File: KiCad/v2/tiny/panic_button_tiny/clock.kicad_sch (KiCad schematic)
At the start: 6 parts, among them Y3 C3E40000121010X, Y4 CTS3-32.768-12.5-20-R

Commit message: [UPDATE] the schematics annotations
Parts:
- renumbered C15 to C11, C16 to C12, C17 to C13, C18 to C14, Y3 to Y1, Y4 to Y2
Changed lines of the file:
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@@
 		(dnp no)
 		(fields_autoplaced yes)
-		(property "Reference" "C16"
+		(property "Reference" "C12"
 			(at 34.2963 63.5 90)
 			(show_name no)
@@
 			(project "panic_button_tiny"
 				(path "/c4eb92e9-b42f-4db0-b1d9-0ef70f7ca601/525ab16f-d6f3-4728-a011-f4f1ced9fd5e/8e1dfb47-dddf-402c-b136-8c72d0253a57"
-					(reference "C16")
+					(reference "C12")
 					(unit 1)
 				)
@@
 		(in_pos_files yes)
 		(dnp no)
-		(property "Reference" "Y3"
+		(property "Reference" "Y1"
 			(at 38.1 44.45 0)
 			(show_name no)
@@
 			(project "panic_button_tiny"
 				(path "/c4eb92e9-b42f-4db0-b1d9-0ef70f7ca601/525ab16f-d6f3-4728-a011-f4f1ced9fd5e/8e1dfb47-dddf-402c-b136-8c72d0253a57"
-					(reference "Y3")
+					(reference "Y1")
 					(unit 1)
 				)
@@
 		(dnp no)
 		(fields_autoplaced yes)
-		(property "Reference" "#PWR074"
+		(property "Reference" "#PWR072"
 			(at 38.1 83.82 0)
 			(hide yes)
@@
 			(project "panic_button_tiny"
 				(path "/c4eb92e9-b42f-4db0-b1d9-0ef70f7ca601/525ab16f-d6f3-4728-a011-f4f1ced9fd5e/8e1dfb47-dddf-402c-b136-8c72d0253a57"
-					(reference "#PWR074")
+					(reference "#PWR072")
 					(unit 1)
 				)
@@
 		(dnp no)
 		(fields_autoplaced yes)
-		(property "Reference" "C18"
+		(property "Reference" "C14"
 			(at 45.7263 27.94 90)
 			(show_name no)
@@
 			(project "panic_button_tiny"
 				(path "/c4eb92e9-b42f-4db0-b1d9-0ef70f7ca601/525ab16f-d6f3-4728-a011-f4f1ced9fd5e/8e1dfb47-dddf-402c-b136-8c72d0253a57"
-					(reference "C18")
+					(reference "C14")
 					(unit 1)
 				)
@@
 		(in_pos_files yes)
 		(dnp no)
-		(property "Reference" "Y4"
+		(property "Reference" "Y2"
 			(at 39.37 23.368 0)
 			(show_name no)
@@
 			(project "panic_button_tiny"
 				(path "/c4eb92e9-b42f-4db0-b1d9-0ef70f7ca601/525ab16f-d6f3-4728-a011-f4f1ced9fd5e/8e1dfb47-dddf-402c-b136-8c72d0253a57"
-					(reference "Y4")
+					(reference "Y2")
 					(unit 1)
 				)
@@
 		(dnp no)
 		(fields_autoplaced yes)
-		(property "Reference" "#PWR075"
+		(property "Reference" "#PWR073"
 			(at 39.37 33.02 0)
 			(hide yes)
@@
 			(project "panic_button_tiny"
 				(path "/c4eb92e9-b42f-4db0-b1d9-0ef70f7ca601/525ab16f-d6f3-4728-a011-f4f1ced9fd5e/8e1dfb47-dddf-402c-b136-8c72d0253a57"
-					(reference "#PWR075")
+					(reference "#PWR073")
 					(unit 1)
 				)
@@
 		(dnp no)
 		(fields_autoplaced yes)
-		(property "Reference" "C15"
+		(property "Reference" "C11"
 			(at 33.0263 27.94 90)
 			(show_name no)
@@
 			(project "panic_button_tiny"
 				(path "/c4eb92e9-b42f-4db0-b1d9-0ef70f7ca601/525ab16f-d6f3-4728-a011-f4f1ced9fd5e/8e1dfb47-dddf-402c-b136-8c72d0253a57"
-					(reference "C15")
+					(reference "C11")
 					(unit 1)
 				)
@@
 		(dnp no)
 		(fields_autoplaced yes)
-		(property "Reference" "C17"
+		(property "Reference" "C13"
 			(at 41.9163 63.5 90)
 			(show_name no)
@@
 			(project "panic_button_tiny"
 				(path "/c4eb92e9-b42f-4db0-b1d9-0ef70f7ca601/525ab16f-d6f3-4728-a011-f4f1ced9fd5e/8e1dfb47-dddf-402c-b136-8c72d0253a57"
-					(reference "C17")
+					(reference "C13")
 					(unit 1)
 				)

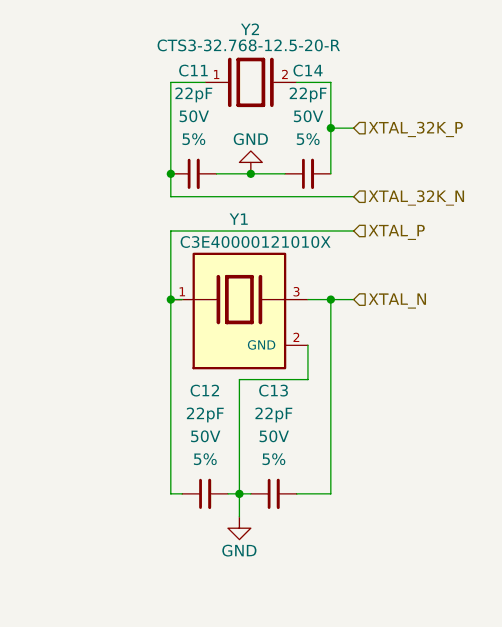
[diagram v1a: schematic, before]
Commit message: [UPDATE] connections in the schematic to better represent the logic flow
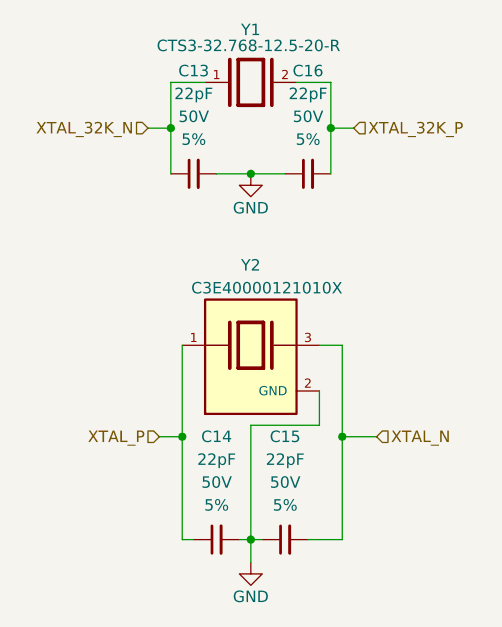
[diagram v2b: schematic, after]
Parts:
- renumbered C11 to C13, C12 to C14, C13 to C15, C14 to C16, Y2 to Y1, Y1 to Y2
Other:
- moved on the sheet: C14, C15, Y2
